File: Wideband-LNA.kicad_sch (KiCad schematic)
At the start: 24 parts, among them J1 RF-IN, J2 RF-OUT, J3 DC-IN, U1 TQP3M9037, U2 MC78L05

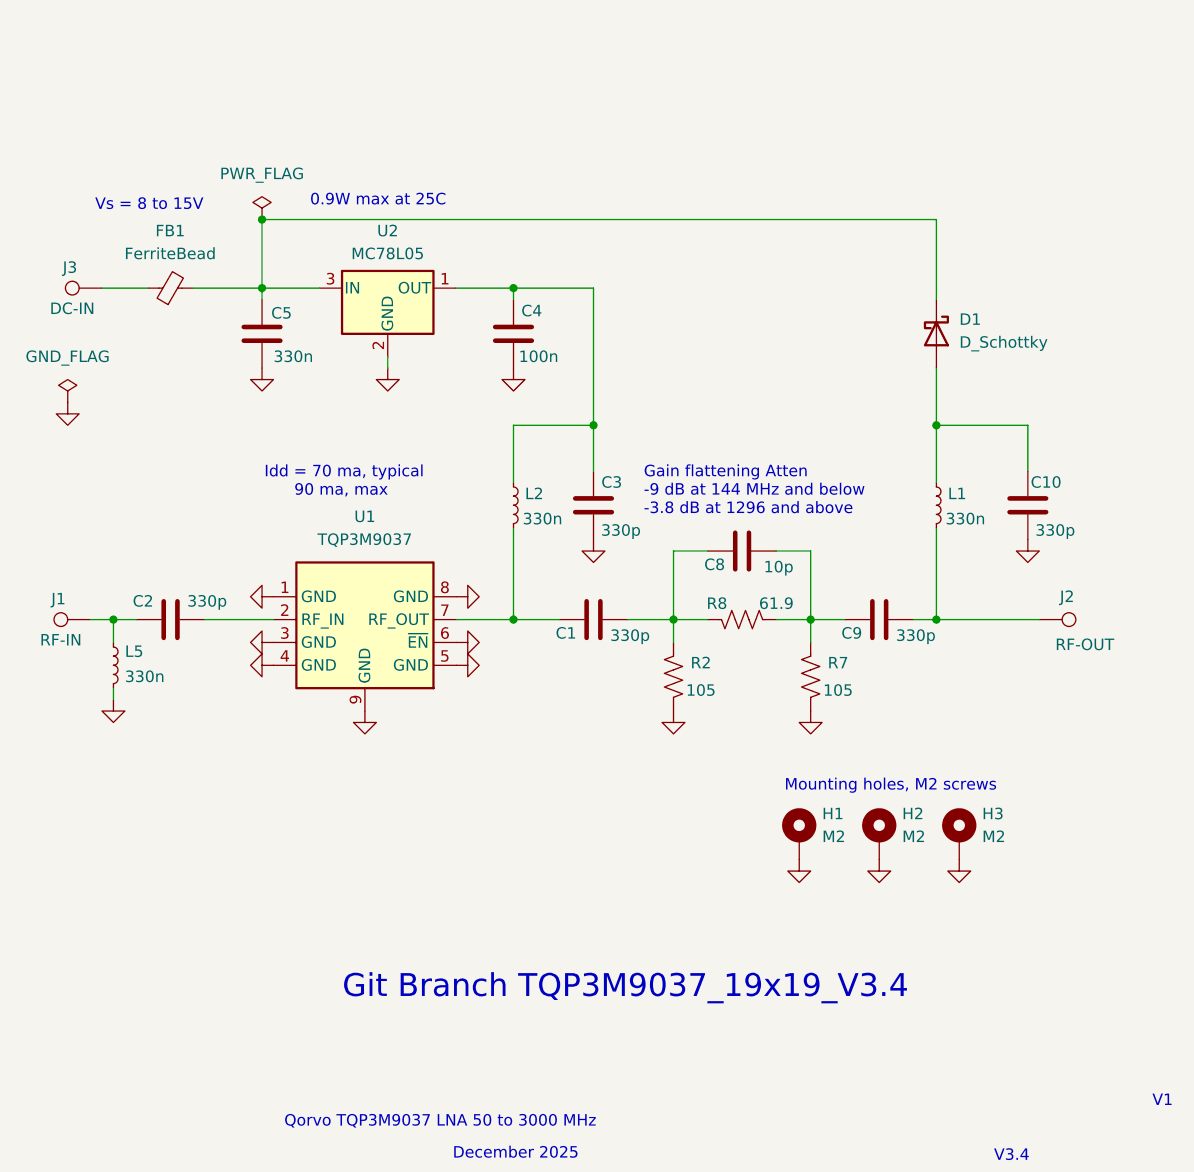
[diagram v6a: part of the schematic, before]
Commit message: Released for production at jlcpcb on Jan 5, 2026 Double checked the jlcpcb tool component selection from LCSC stock
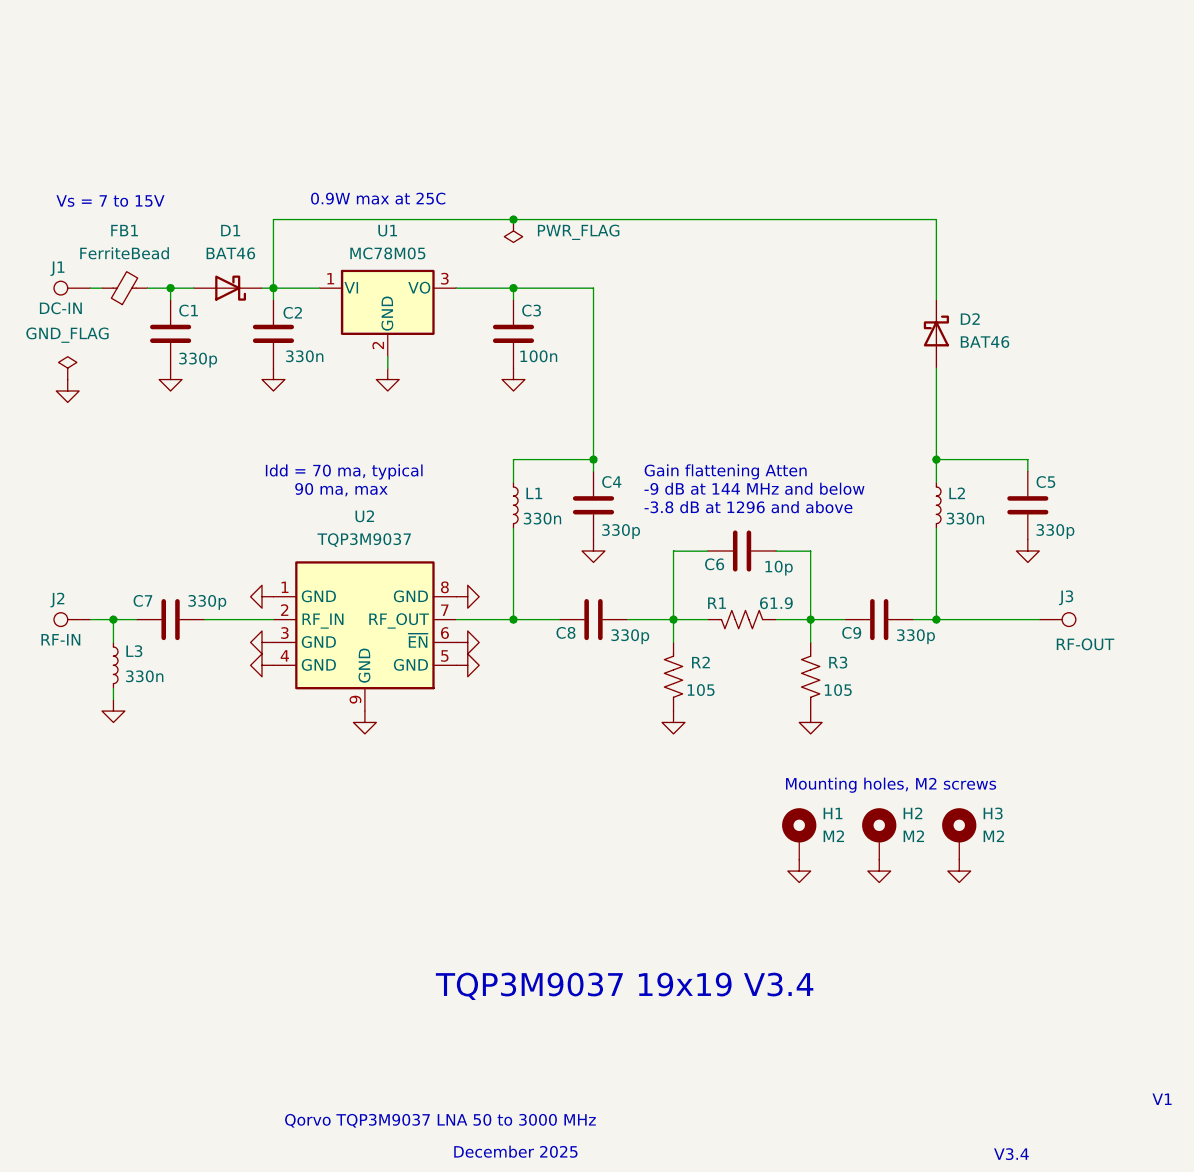
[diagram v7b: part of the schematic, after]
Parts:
- removed U2: MC78L05, Package_TO_SOT_SMD:TO-252-2, symbol Regulator_Linear:MC78L05_SOT89
- added C1: 330p, Capacitor_SMD:C_0402_1005Metric, symbol Device:C
- added D1: BAT46, Diode_SMD:D_SOD-523, symbol Device:D_Schottky
- added U1: MC78M05, Package_TO_SOT_SMD:TO-252-2, symbol Regulator_Linear:LM78M05_TO252
- C2: renamed from C5; LCSC C1525 -> C282682
- C3: renamed from C4; footprint Capacitor_SMD:C_0603_1608Metric -> Capacitor_SMD:C_0402_1005Metric
- C4: renamed from C3; footprint Capacitor_SMD:C_0603_1608Metric -> Capacitor_SMD:C_0402_1005Metric
- C5: renamed from C10; footprint Capacitor_SMD:C_0603_1608Metric -> Capacitor_SMD:C_0402_1005Metric
- C6: renamed from C8; LCSC C1546 -> C1634
- C7: renamed from C2; LCSC C1546 -> C1664
- C8: renamed from C1; LCSC C1546 -> C1664
- C9: LCSC C1546 -> C1664
- D2: renamed from D1; value D_Schottky -> BAT46; LCSC (none) -> C22466367
- FB1: LCSC C1017 -> C1002
- L1: renamed from L2; LCSC C405073 -> C6808006
- L2: renamed from L1; LCSC C405073 -> C6808006
- R1: renamed from R8; LCSC C11702 -> C482904
- R2: LCSC C11702 -> C227541
- R3: renamed from R7; LCSC C11702 -> C227541
- U2: renamed from U1; LCSC (none) -> C415712
- renumbered J3 to J1, J1 to J2, J2 to J3, L5 to L3
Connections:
- net GND: now also C1.2, U1.2 (GND)
- net at C2.1, D2.1 (K): now also D1.1 (K), U1.1 (VI); no longer FB1.2
- net at C3.1, C4.1, L1.1: now also U1.3 (VO)
- new net: C1.1, D1.2 (A), FB1.2
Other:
- note added: "TQP3M9037 19x19 V3.4"
- note added: "Vs = 7 to 15V"
- note removed: "Git Branch TQP3M9037_19x19_V3.4"
- note removed: "Vs = 8 to 15V"
- moved on the sheet: C2, FB1, J1

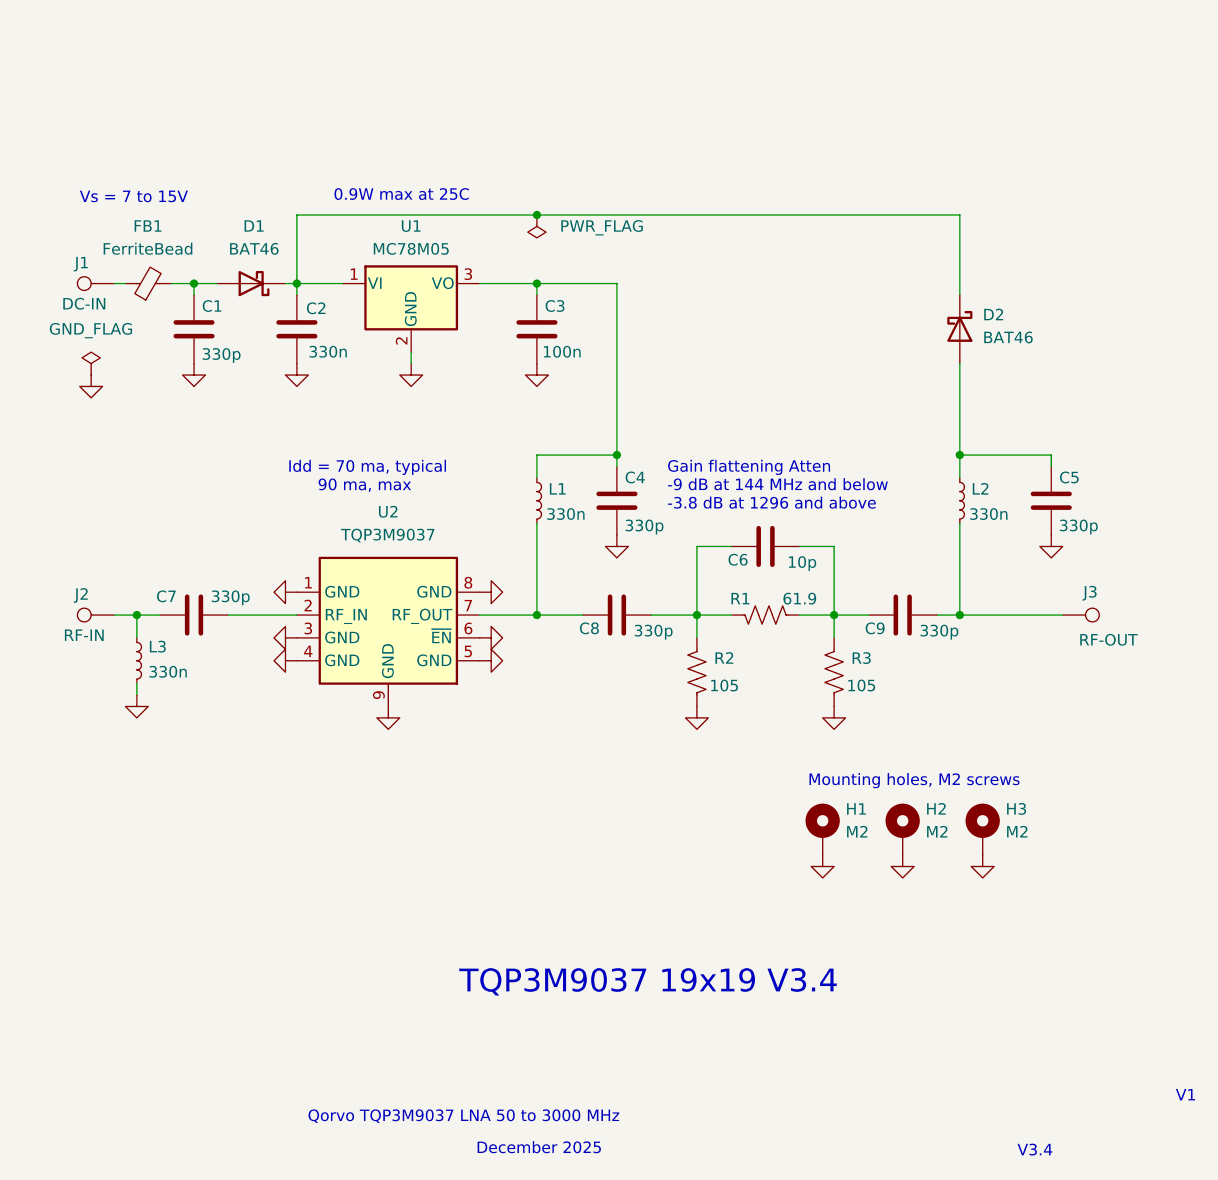
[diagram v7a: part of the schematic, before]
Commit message: Stop tracking JLCPCB generated files
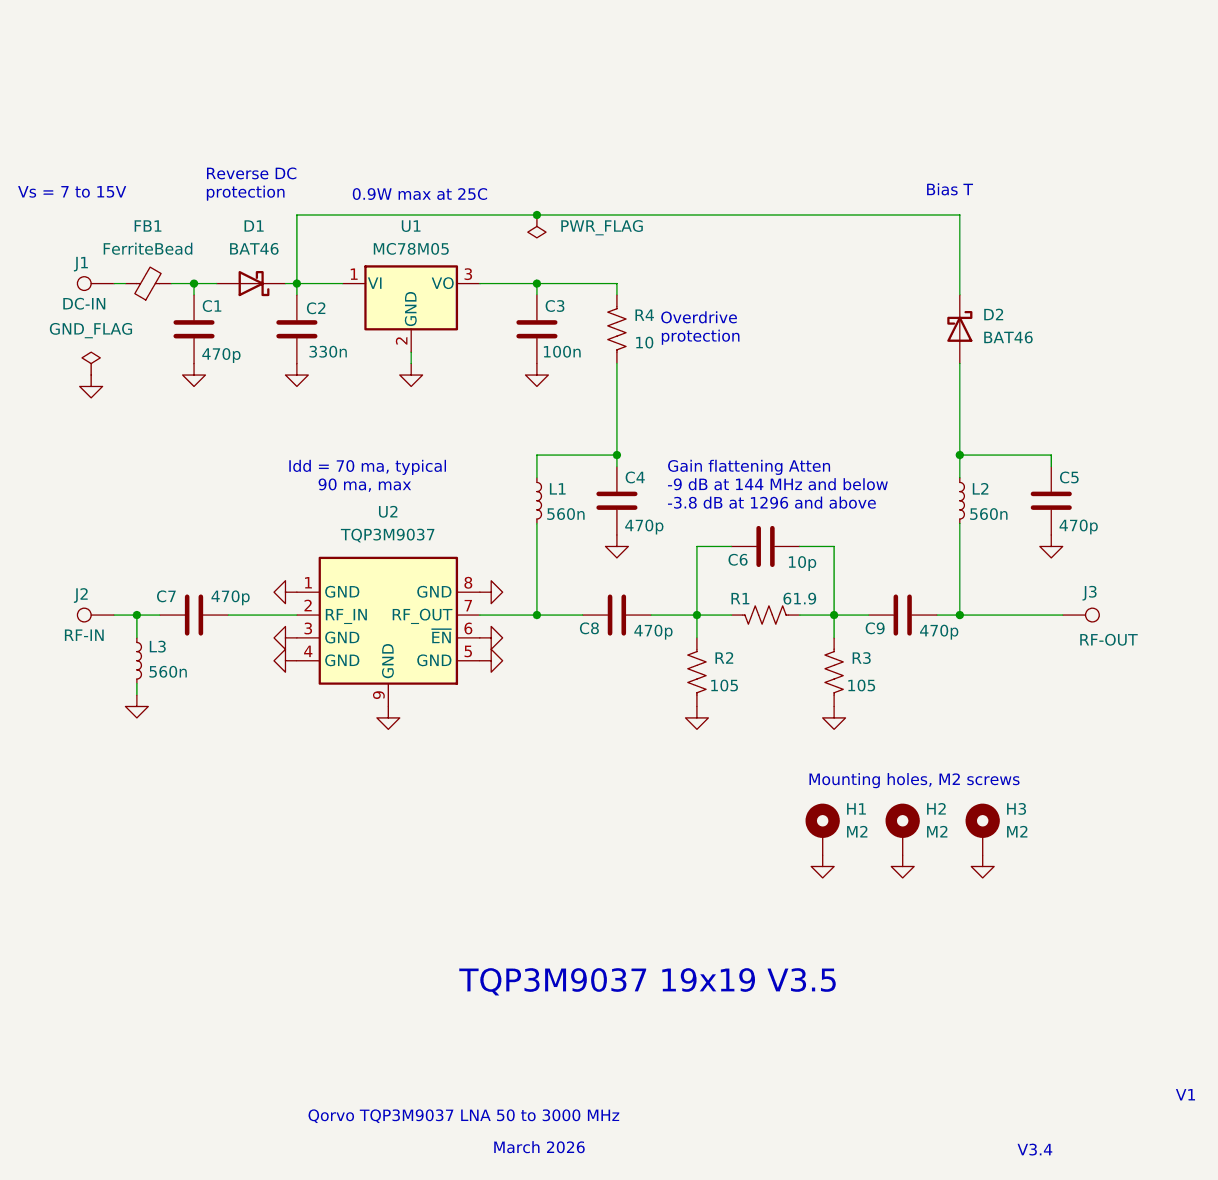
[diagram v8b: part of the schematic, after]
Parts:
- added R4: 10, Resistor_SMD:R_0402_1005Metric, symbol Device:R_US
- C1, C4, C5: value 330p -> 470p; LCSC C1546 -> C20069335
- C2: footprint Capacitor_SMD:C_0603_1608Metric -> Capacitor_SMD:C_0402_1005Metric
- C3: LCSC C52923 -> C1525
- C7, C8, C9: value 330p -> 470p; footprint Capacitor_SMD:C_0603_1608Metric -> Capacitor_SMD:C_0402_1005Metric; LCSC C1664 -> C20069335
- L1, L2: value 330n -> 560n; LCSC C6808006 -> C6808023
- L3: value 330n -> 560n; LCSC C405073 -> C6808023
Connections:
- net at C4.1, L1.1: now also R4.2; no longer C3.1, U1.3 (VO)
- new net: C3.1, R4.1, U1.3 (VO)
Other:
- note added: "Bias T"
- note added: "March 2026"
- note added: "Overdrive protection"
- note added: "Reverse DC protection"
- note added: "TQP3M9037 19x19 V3.5"
- note removed: "December 2025"
- note removed: "TQP3M9037 19x19 V3.4"
